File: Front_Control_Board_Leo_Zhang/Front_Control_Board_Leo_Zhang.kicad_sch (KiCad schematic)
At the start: 53 parts, among them J1 22035035, J10 430450200, J11 430450200, J12 430450200, J2 Molex Micro-Fit 4 Pin, J3 430450200, J4 430450200, J5 430450200, J6 430450200, J7 22035035, J8 22035035, J9 22035035, Q1 PSMN5R2-60YL, Q2 PSMN5R2-60YL, Q3 PSMN5R2-60YL, Q4 PSMN5R2-60YL, Q5 PSMN5R2-60YL, Q6 PSMN5R2-60YL, U2 ADS1118IDGS, U3 MCP2562-E-P, U5 UA78M05QDCYRG4Q1

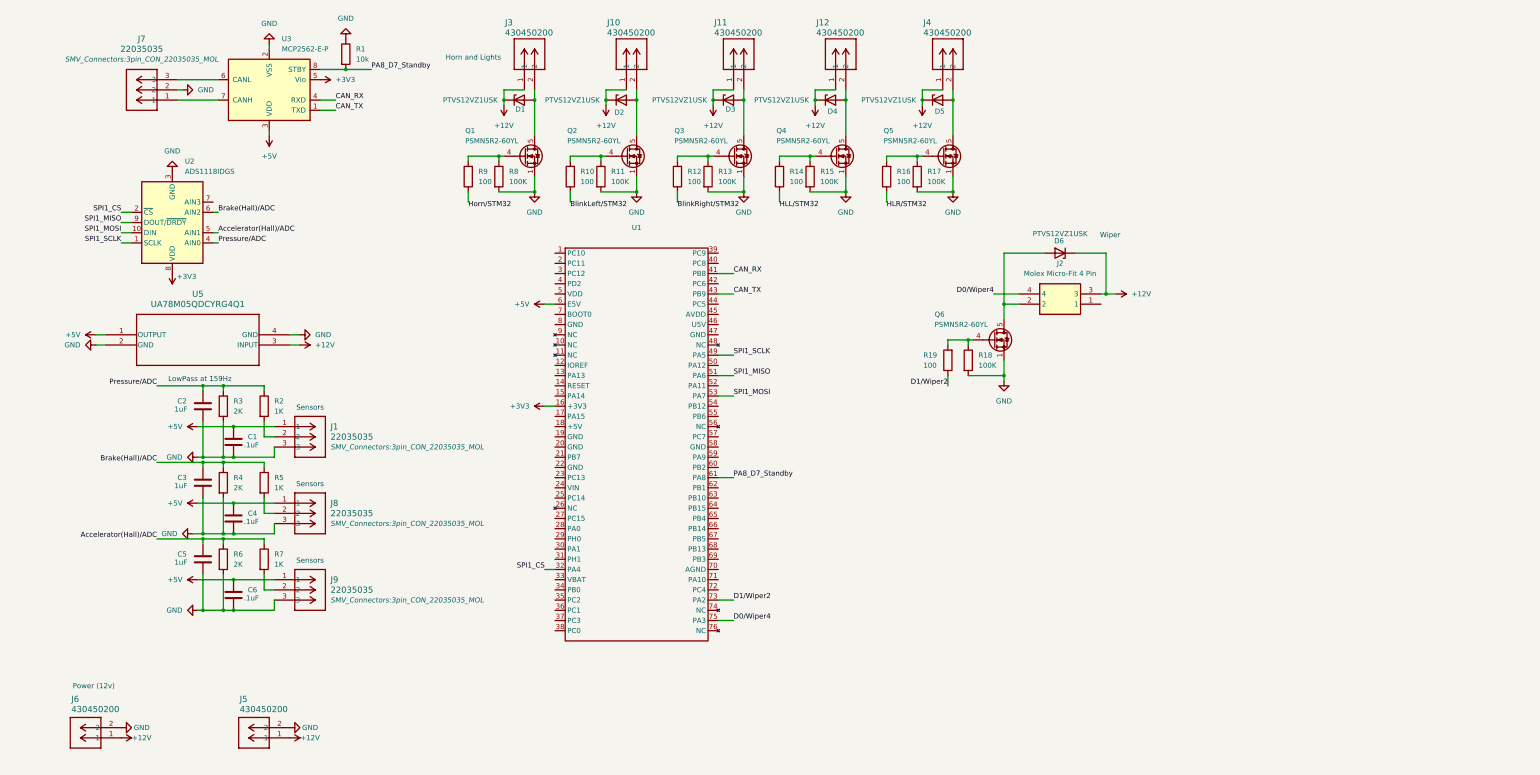
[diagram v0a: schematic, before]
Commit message: Decoupling, test points, TODO: if can (voltage follower)
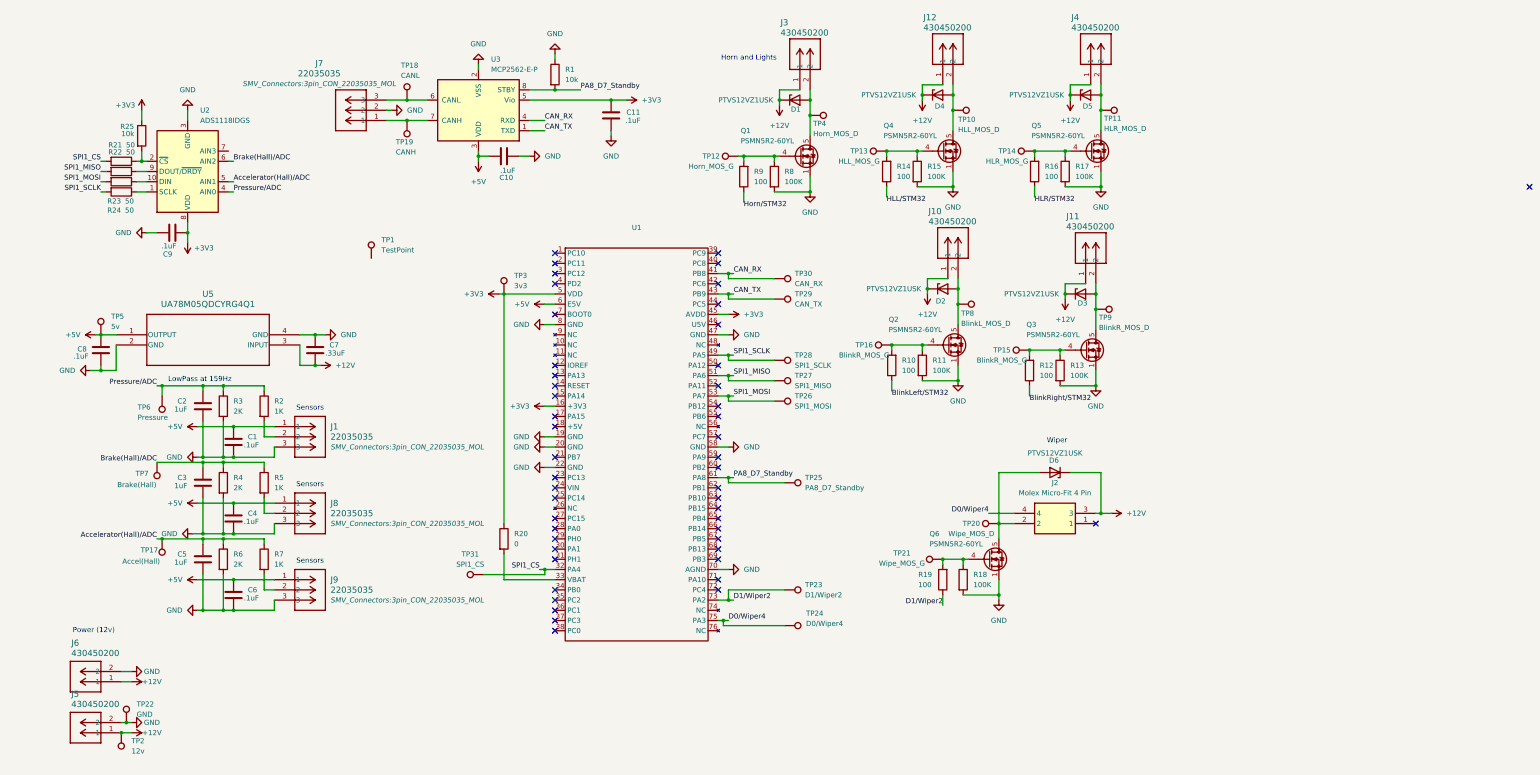
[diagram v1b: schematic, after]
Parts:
- added C10, C11, C8, C9: .1uF, symbol Device:C
- added C7: .33uF, symbol Device:C
- added R20: 0, symbol Device:R
- added R21, R22, R23, R24: 50, symbol Device:R
- added R25: 10k, symbol Device:R
- added TP1: TestPoint, TestPoint:TestPoint_Pad_D1.0mm, symbol Connector:TestPoint
- added TP10: HLL_MOS_D, TestPoint:TestPoint_Pad_D1.0mm, symbol Connector:TestPoint
- added TP11: HLR_MOS_D, TestPoint:TestPoint_Pad_D1.0mm, symbol Connector:TestPoint
- added TP12: Horn_MOS_G, TestPoint:TestPoint_Pad_D1.0mm, symbol Connector:TestPoint
- added TP13: HLL_MOS_G, TestPoint:TestPoint_Pad_D1.0mm, symbol Connector:TestPoint
- added TP14: HLR_MOS_G, TestPoint:TestPoint_Pad_D1.0mm, symbol Connector:TestPoint
- added TP15, TP16: BlinkR_MOS_G, TestPoint:TestPoint_Pad_D1.0mm, symbol Connector:TestPoint
- added TP17: Accel(Hall), TestPoint:TestPoint_Pad_D1.0mm, symbol Connector:TestPoint
- added TP18: CANL, TestPoint:TestPoint_Pad_D1.0mm, symbol Connector:TestPoint
- added TP19: CANH, TestPoint:TestPoint_Pad_D1.0mm, symbol Connector:TestPoint
- added TP2: 12v, TestPoint:TestPoint_Pad_D1.0mm, symbol Connector:TestPoint
- added TP20: Wipe_MOS_D, TestPoint:TestPoint_Pad_D1.0mm, symbol Connector:TestPoint
- added TP21: Wipe_MOS_G, TestPoint:TestPoint_Pad_D1.0mm, symbol Connector:TestPoint
- added TP22: GND, TestPoint:TestPoint_Pad_D1.0mm, symbol Connector:TestPoint
- added TP23: D1/Wiper2, TestPoint:TestPoint_Pad_D1.0mm, symbol Connector:TestPoint
- added TP24: D0/Wiper4, TestPoint:TestPoint_Pad_D1.0mm, symbol Connector:TestPoint
- added TP25: PA8_D7_Standby, TestPoint:TestPoint_Pad_D1.0mm, symbol Connector:TestPoint
- added TP26: SPI1_MOSI, TestPoint:TestPoint_Pad_D1.0mm, symbol Connector:TestPoint
- added TP27: SPI1_MISO, TestPoint:TestPoint_Pad_D1.0mm, symbol Connector:TestPoint
- added TP28: SPI1_SCLK, TestPoint:TestPoint_Pad_D1.0mm, symbol Connector:TestPoint
- added TP29: CAN_TX, TestPoint:TestPoint_Pad_D1.0mm, symbol Connector:TestPoint
- added TP3: 3v3, TestPoint:TestPoint_Pad_D1.0mm, symbol Connector:TestPoint
- added TP30: CAN_RX, TestPoint:TestPoint_Pad_D1.0mm, symbol Connector:TestPoint
- added TP31: SPI1_CS, TestPoint:TestPoint_Pad_D1.0mm, symbol Connector:TestPoint
- added TP4: Horn_MOS_D, TestPoint:TestPoint_Pad_D1.0mm, symbol Connector:TestPoint
- added TP5: 5v, TestPoint:TestPoint_Pad_D1.0mm, symbol Connector:TestPoint
- added TP6: Pressure, TestPoint:TestPoint_Pad_D1.0mm, symbol Connector:TestPoint
- added TP7: Brake(Hall), TestPoint:TestPoint_Pad_D1.0mm, symbol Connector:TestPoint
- added TP8: BlinkL_MOS_D, TestPoint:TestPoint_Pad_D1.0mm, symbol Connector:TestPoint
- added TP9: BlinkR_MOS_D, TestPoint:TestPoint_Pad_D1.0mm, symbol Connector:TestPoint
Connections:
- net +12V: now also C7.2, TP2.1
- net +3V3: now also U1.45 (AVDD), U1.5 (VDD), C11.1, C9.2, R20.1, R25.1, TP3.1
- net +5V: now also C10.1, C8.1, TP5.1
- net Accelerator(Hall)/ADC: now also TP17.1
- net Brake(Hall)/ADC: now also TP7.1
- net CAN_RX: now also TP30.1
- net CAN_TX: now also TP29.1
- net D0/Wiper4: now also TP24.1
- net D1/Wiper2: now also TP23.1
- net GND: now also U1.19 (GND), U1.20 (GND), U1.22 (GND), U1.47 (GND), U1.58 (GND), U1.70 (AGND), U1.8 (GND), C10.2, C11.2, C7.1, C8.2, C9.1, TP22.1
- net PA8_D7_Standby: now also TP25.1
- net Pressure/ADC: now also TP6.1
- net SPI1_CS: now also R21.2, TP31.1; no longer U2.2 (~{CS})
- net SPI1_MISO: now also R22.2, TP27.1; no longer U2.9 (DOUT/~{DRDY})
- net SPI1_MOSI: now also R23.2, TP26.1; no longer U2.10 (DIN)
- net SPI1_SCLK: now also R24.2, TP28.1; no longer U2.1 (SCLK)
- net at Q6.4 (G), R18.1, R19.2: now also TP21.1
- net at Q3.4 (G), R12.2, R13.1: now also TP15.1
- net at Q4.4 (G), R14.2, R15.1: now also TP13.1
- net at D5.2 (A), J4.2, Q5.5 (D): now also TP11.1
- net at Q1.4 (G), R8.1, R9.2: now also TP12.1
- net at Q5.4 (G), R16.2, R17.1: now also TP14.1
- net at D3.2 (A), J11.2, Q3.5 (D): now also TP9.1
- net at D2.2 (A), J10.2, Q2.5 (D): now also TP8.1
- net at D6.2 (A), J2.2, Q6.5 (D): now also TP20.1
- net at Q2.4 (G), R10.2, R11.1: now also TP16.1
- net at D4.2 (A), J12.2, Q4.5 (D): now also TP10.1
- net at D1.2 (A), J3.2, Q1.5 (D): now also TP4.1
- net at J7.1, U3.7 (CANH): now also TP19.1
- net at J7.3, U3.6 (CANL): now also TP18.1
- net at U1.33 (VBAT): now also R20.2
- new net: R23.1, U2.10 (DIN)
- new net: R21.1, R25.2, U2.2 (~{CS})
- new net: R24.1, U2.1 (SCLK)
- new net: R22.1, U2.9 (DOUT/~{DRDY})
- no-connect marks 0 -> 49
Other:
- moved on the sheet: D1, D2, D3, D4, D5, D6, J10, J11, J12, J2, J3, J4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

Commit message: implemented initial feedback
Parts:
- added C12, C13, C14: .1uF, symbol Device:C
- added R26, R27, R28: 100, symbol Device:R
- added TP32: P_VFout, TestPoint:TestPoint_Pad_D1.0mm, symbol Connector:TestPoint
- added TP33: B_VFout, TestPoint:TestPoint_Pad_D1.0mm, symbol Connector:TestPoint
- added TP34: A_VFout, TestPoint:TestPoint_Pad_D1.0mm, symbol Connector:TestPoint
- added U4, U6, U7: MCP6286T-E/OT, SMV_ICs:SOT-23-5_MC_MCH, symbol SMV_Custom:MCP6286T-E_OT
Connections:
- net +3V3: now also C12.2, C13.2, C14.2, U4.5 (VDD), U6.5 (VDD), U7.5 (VDD)
- net GND: now also C12.1, C13.1, C14.1, U4.2 (VSS), U6.2 (VSS), U7.2 (VSS)
- net Accelerator(Hall)/ADC renamed Accelerator(Hall)/VFin
- net Accelerator(Hall)/VFin: now also R28.1; no longer U2.5 (AIN1)
- net Brake(Hall)/ADC renamed Brake(Hall)/VFin
- net Brake(Hall)/VFin: now also R27.1; no longer U2.6 (AIN2)
- net Pressure/ADC renamed Pressure/VFin
- net Pressure/VFin: now also R26.1; no longer U2.4 (AIN0)
- new net: R28.2, U7.3 (VIN+)
- new net: R26.2, U4.3 (VIN+)
- new net: R27.2, U6.3 (VIN+)
- new net Accelerator(Hall)/VFout: TP34.1, U2.5 (AIN1), U7.1 (VOUT), U7.4 (VIN-)
- new net Brake(Hall)/VFout: TP33.1, U2.6 (AIN2), U6.1 (VOUT), U6.4 (VIN-)
- new net Pressure/VFout: TP32.1, U2.4 (AIN0), U4.1 (VOUT), U4.4 (VIN-)
- no-connect marks 49 -> 50
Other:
- moved on the sheet: C1, C10, C11, C2, C3, C4, C5, C6, C7, C8, C9, D6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

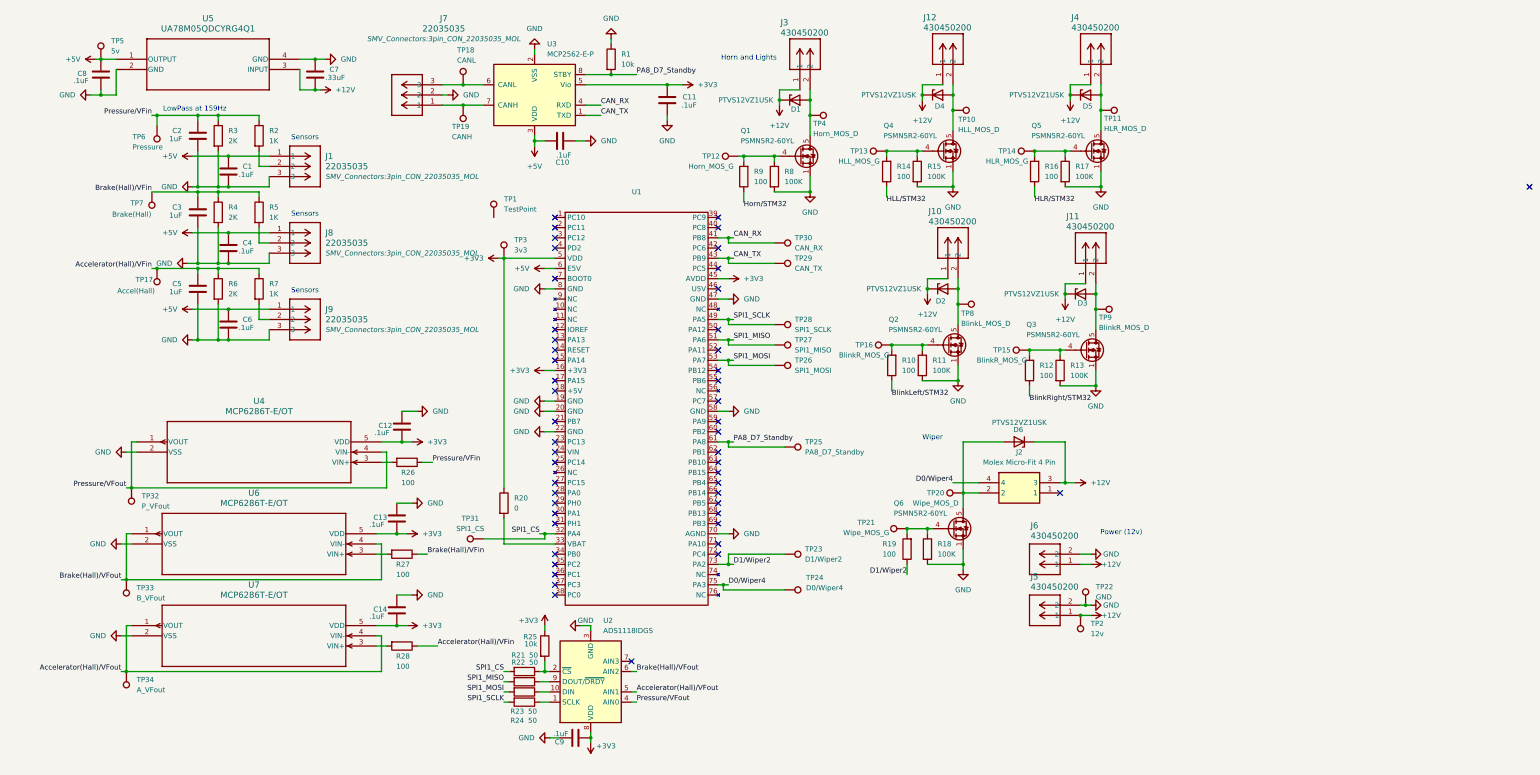
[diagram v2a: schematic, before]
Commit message: fixed missing ratsnests, updating from MSI laptop
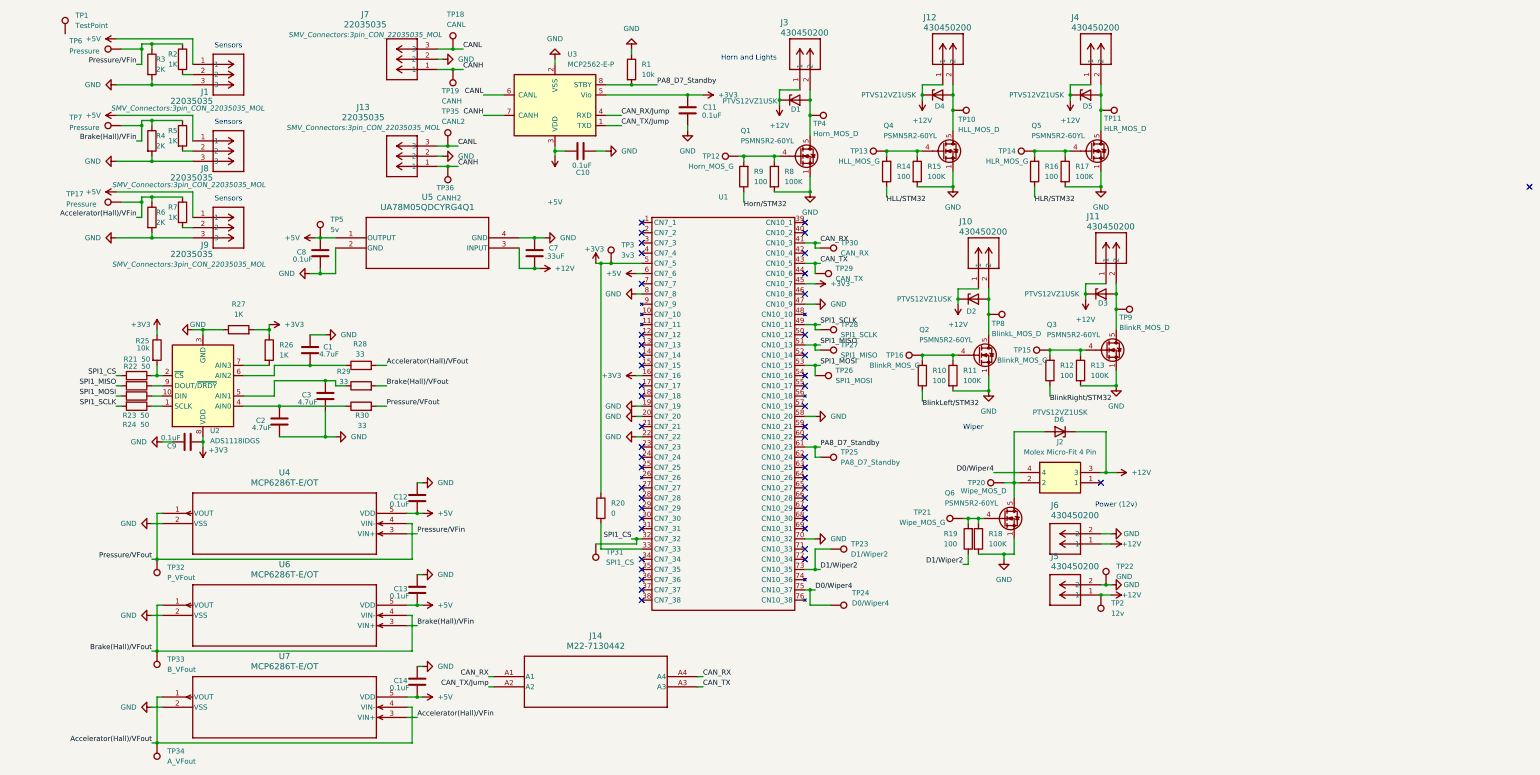
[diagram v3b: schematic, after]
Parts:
- removed C4, C6: .1uF, symbol Device:C
- removed C5: 1uF, symbol Device:C
- added J13: 22035035, SMV_Connectors:3pin_CON_22035035_MOL, symbol SMV_Custom:3-pin Mini Molex Spox
- added J14: M22-7130442, Jumperz:M22-7130442_TYC, symbol Jumpers:M22-7130442
- added R29, R30: 33, Resistor_SMD:R_0805_2012Metric, symbol Device:R
- added TP35: CANL2, TestPoint:TestPoint_Pad_D1.0mm, symbol Connector:TestPoint
- added TP36: CANH2, TestPoint:TestPoint_Pad_D1.0mm, symbol Connector:TestPoint
- C1: value .1uF -> 4.7uF; footprint (none) -> Capacitor_SMD:C_0805_2012Metric
- C10, C11, C12, C13, C14, C8, C9: value .1uF -> 0.1uF; footprint (none) -> Capacitor_SMD:C_0805_2012Metric
- C2, C3: value 1uF -> 4.7uF; footprint (none) -> Capacitor_SMD:C_0805_2012Metric
- C7: footprint (none) -> Capacitor_SMD:C_0805_2012Metric
- R1, R10, R11, R12, R13, R14, R15, R16, R17, R18, R19, R2, R20, R21, R22, R23, R24, R25, R3, R4, R5, R6, R7, R8, R9: footprint (none) -> Resistor_SMD:R_0805_2012Metric
- R26, R27: value 100 -> 1K; footprint (none) -> Resistor_SMD:R_0805_2012Metric
- R28: value 100 -> 33; footprint (none) -> Resistor_SMD:R_0805_2012Metric
- TP17: value Accel(Hall) -> Pressure
- TP7: value Brake(Hall) -> Pressure
- U1: footprint (none) -> SMV_ICs:MODULE_NUCLEO-F446RE
- U2: footprint (none) -> SMV_ICs:DGS0010A_N
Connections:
- net +3V3: now also R26.1, R27.2; no longer C12.2, C13.2, C14.2, U4.5 (VDD), U6.5 (VDD), U7.5 (VDD)
- net +5V: now also C12.2, C13.2, C14.2, U4.5 (VDD), U6.5 (VDD), U7.5 (VDD); no longer C1.1
- net Accelerator(Hall)/VFin: now also U7.3 (VIN+); no longer R28.1
- net Accelerator(Hall)/VFout: now also R28.2; no longer U2.5 (AIN1)
- net Brake(Hall)/VFin: now also U6.3 (VIN+); no longer C3.1, R27.1
- net Brake(Hall)/VFout: now also R29.2; no longer U2.6 (AIN2)
- net CAN_RX: now also J14.A1, J14.A4; no longer U3.4 (RXD)
- net CAN_TX: now also J14.A3; no longer U3.1 (TXD)
- net GND: now also C1.1, R27.1, J13.2; no longer C1.2
- net Pressure/VFin: now also U4.3 (VIN+); no longer C2.1, R26.1
- net Pressure/VFout: now also R30.2; no longer U2.4 (AIN0)
- net at R26.2: now also U2.7 (AIN3); no longer U4.3 (VIN+)
- net CANH: now reaches J7.1, TP19.1, U3.7 (CANH)
- net CANH: now also J13.1, TP36.1
- net CANL: now reaches J7.3, TP18.1, U3.6 (CANL)
- net CANL: now also J13.3, TP35.1
- new net: C2.1, R30.1, U2.4 (AIN0)
- new net: C3.1, R29.1, U2.5 (AIN1)
- new net: C1.2, R28.1, U2.6 (AIN2)
- new net CAN_RX/Jump: U3.4 (RXD)
- new net CAN_TX/Jump: J14.A2, U3.1 (TXD)
- no-connect marks 50 -> 49
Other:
- note removed: "LowPass at 159Hz"
- moved on the sheet: C10, C11, C12, C13, C14, C7, C8, C9, D2, D3, D6, J1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

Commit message: Done w first draft! waiting for feedback
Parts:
- added J15: M22-7130442, SMV_Connectors:M22-7130442_TYC, symbol Jumpers:M22-7130442
- added TP37: BlinkRSig, TestPoint:TestPoint_Pad_D1.0mm, symbol Connector:TestPoint
- added TP38: HLRSig, TestPoint:TestPoint_Pad_D1.0mm, symbol Connector:TestPoint
- added TP39: HLLSig, TestPoint:TestPoint_Pad_D1.0mm, symbol Connector:TestPoint
- added TP40: HornSig, TestPoint:TestPoint_Pad_D1.0mm, symbol Connector:TestPoint
- J14: footprint Jumperz:M22-7130442_TYC -> SMV_Connectors:M22-7130442_TYC
- TP1: value TestPoint -> BlinkLSig
- TP16: value BlinkR_MOS_G -> BlinkL_MOS_G
- TP17: value Pressure -> Accelerator
- TP7: value Pressure -> Brake
- U3: footprint Package_DIP:DIP-8_W7.62mm -> Package_DIP:SMDIP-8_W7.62mm
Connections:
- net BlinkLeft/STM32: now also TP1.1, U1.59 (PA9)
- net BlinkRight/STM32: now also U1.57 (PC7), TP37.1
- net CAN_RX: now also J15.4 (A4); no longer J14.A1, J14.A4
- net CAN_RX/Jump: now also J14.1 (A1)
- net CAN_TX: now also J15.1 (A1); no longer J14.A3
- net CAN_TX/Jump: now also J14.4 (A4); no longer J14.A2
- net HLL/STM32: now also U1.53 (PA7), TP39.1
- net HLR/STM32: now also U1.55 (PB6), TP38.1
- net Horn/STM32: now also U1.51 (PA6), TP40.1
- net PA8_D7_Standby: now also U1.71 (PA10); no longer U1.61 (CN10_23)
- net SPI1_CS: now also U1.4 (PD2); no longer U1.32 (CN7_32)
- net SPI1_MISO: now also U1.2 (PC11); no longer U1.51 (CN10_13)
- net SPI1_MOSI: now also U1.3 (PC12); no longer U1.53 (CN10_15)
- net SPI1_SCLK: now also U1.1 (PC10); no longer U1.49 (CN10_11)
- no-connect marks 49 -> 44
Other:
- moved on the sheet: TP23, TP25, TP26, TP27, TP28, TP3, TP31
